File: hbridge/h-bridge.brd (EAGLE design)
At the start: 44.5 x 44.5 mm, 8 parts

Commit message: add connector parts
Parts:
- added R1, R2, R3, R4: (no value), resistor:R0603
- added U$2: JST-PH8-SMD-90, jst-ph:JST-PH-SMD-90*
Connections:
- new net N$2: R2.1, R3.1, R4.1, U$2.P$1
- net ENABLE: now also R1.2, U$2.P$8
- net GND: now also R1.1, R4.2
- net M1_DIR: now also U$2.P$6
- net M1_MOVE: now also U$2.P$7
- net M2_DIR: now also U$2.P$4
- net M2_MOVE: now also U$2.P$5
- net M3_DIR: now also U$2.P$2
- net M3_MOVE: now also U$2.P$3
- net V_RUN: now also R2.2, R3.2
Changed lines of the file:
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@@
 <element name="CHARGE" library="con-molex-micro-fit-3_0" package="43045-0206" value="" x="2.54" y="10.795" rot="R270"/>
 <element name="U$1" library="wolfbot" package="WSP1-T2-M6" value="ESWITCH-WSP1" x="2.54" y="29.21"/>
+<element name="R1" library="resistor" package="R0603" value="" x="-20.32" y="-7.62"/>
+<element name="U$2" library="jst-ph" package="JST-PH-SMD-90*" value="JST-PH8-SMD-90" x="-17.78" y="-17.78"/>
+<element name="R2" library="resistor" package="R0603" value="" x="-20.32" y="-22.86"/>
+<element name="R3" library="resistor" package="R0603" value="" x="-20.32" y="-27.94"/>
+<element name="R4" library="resistor" package="R0603" value="" x="-20.32" y="-33.02"/>
 </elements>
 <signals>
@@
 <wire x1="36.44" y1="24.765" x2="34.925" y2="26.5975" width="0.508" layer="1"/>
 <wire x1="34.925" y1="26.5975" x2="34.925" y2="40.005" width="0.508" layer="1"/>
+<contactref element="R1" pad="1"/>
+<contactref element="R4" pad="2"/>
+<wire x1="26.035" y1="30.48" x2="26.035" y2="33.02" width="0" layer="19" extent="1-1"/>
+<wire x1="21.2725" y1="8.89" x2="15.875" y2="9.525" width="0" layer="19" extent="1-1"/>
+<wire x1="23.495" y1="12.065" x2="23.495" y2="9.525" width="0" layer="19" extent="1-1"/>
+<wire x1="23.495" y1="1.905" x2="23.495" y2="4.445" width="0" layer="19" extent="1-1"/>
+<wire x1="23.495" y1="17.145" x2="23.495" y2="12.065" width="0" layer="19" extent="1-1"/>
+<wire x1="36.44" y1="16.51" x2="36.44" y2="24.765" width="0" layer="19" extent="1-1"/>
+<wire x1="-21.17" y1="-7.62" x2="8.01" y2="10.795" width="0" layer="19" extent="1-1"/>
+<wire x1="-19.47" y1="-33.02" x2="-21.17" y2="-7.62" width="0" layer="19" extent="1-1"/>
 </signal>
 <signal name="V+" class="1">
@@
 <wire x1="26.0096" y1="22.9616" x2="26.035" y2="22.86" width="0.254" layer="16"/>
 <via x="11.5062" y="32.0167" extent="1-16" drill="0.508"/>
+<contactref element="R1" pad="2"/>
+<contactref element="U$2" pad="P$8"/>
+<wire x1="-0.83" y1="-13.28" x2="13.8176" y2="20.1168" width="0" layer="19" extent="1-16"/>
+<wire x1="-19.47" y1="-7.62" x2="-0.83" y2="-13.28" width="0" layer="19" extent="1-1"/>
 </signal>
 <signal name="M1_MOVE">
@@
 <wire x1="28.067" y1="15.24" x2="26.416" y2="15.24" width="0.254" layer="16"/>
 <wire x1="18.288" y1="37.9984" x2="18.415" y2="38.1" width="0.254" layer="16"/>
+<contactref element="U$2" pad="P$7"/>
+<wire x1="-2.83" y1="-13.28" x2="6.4897" y2="18.4912" width="0" layer="19" extent="1-16"/>
 </signal>
 <signal name="M1-" class="1">
@@
 <wire x1="27.6352" y1="12.5984" x2="27.813" y2="12.7" width="0.254" layer="16"/>
 <via x="13.6144" y="17.0688" extent="1-16" drill="0.508"/>
+<contactref element="U$2" pad="P$6"/>
+<wire x1="-4.83" y1="-13.28" x2="19.1643" y2="8.128" width="0" layer="19" extent="1-16"/>
 </signal>
 <signal name="M2_DIR">
@@
 <wire x1="27.8384" y1="7.7216" x2="27.813" y2="7.62" width="0.254" layer="1"/>
 <via x="32.512" y="12.5984" extent="1-16" drill="0.508"/>
+<contactref element="U$2" pad="P$4"/>
+<wire x1="-8.83" y1="-13.28" x2="27.813" y2="7.62" width="0" layer="19" extent="1-1"/>
 </signal>
 <signal name="M2+" class="1">
@@
 <wire x1="28.067" y1="10.16" x2="28.6512" y2="10.16" width="0.254" layer="16"/>
 <wire x1="26.2128" y1="25.4" x2="26.035" y2="25.4" width="0.254" layer="16"/>
+<contactref element="U$2" pad="P$5"/>
+<wire x1="-6.83" y1="-13.28" x2="28.067" y2="10.16" width="0" layer="19" extent="1-1"/>
 </signal>
 <signal name="M3_MOVE">
@@
 <wire x1="16.0528" y1="17.0688" x2="15.875" y2="17.145" width="0.254" layer="16"/>
 <via x="21.0185" y="12.5603" extent="1-16" drill="0.508"/>
+<contactref element="U$2" pad="P$3"/>
+<wire x1="19.9771" y1="0.4572" x2="-10.83" y2="-13.28" width="0" layer="19" extent="1-1"/>
 </signal>
 <signal name="M3-" class="1">
@@
 <wire x1="27.6352" y1="2.4384" x2="25.6032" y2="0.4064" width="0.254" layer="16"/>
 <wire x1="27.6352" y1="2.4384" x2="27.813" y2="2.54" width="0.254" layer="16"/>
+<contactref element="U$2" pad="P$2"/>
+<wire x1="15.875" y1="4.445" x2="-12.83" y2="-13.28" width="0" layer="19" extent="1-1"/>
 </signal>
 <signal name="V_RUN" class="1">
@@
 <wire x1="23.368" y1="19.7104" x2="23.495" y2="19.685" width="0.508" layer="16"/>
 <via x="18.8976" y="19.9136" extent="1-16" drill="0.508"/>
+<contactref element="R2" pad="2"/>
+<contactref element="R3" pad="2"/>
+<wire x1="-19.47" y1="-22.86" x2="-19.47" y2="-27.94" width="0" layer="19" extent="1-1"/>
+<wire x1="15.875" y1="1.905" x2="-19.47" y2="-22.86" width="0" layer="19" extent="1-1"/>
 </signal>
 <signal name="V_CHARGE" class="1">
@@
 <via x="8.2296" y="32.8295" extent="1-16" drill="0.508"/>
 </signal>
+<signal name="N$2">
+<contactref element="R2" pad="1"/>
+<contactref element="R3" pad="1"/>
+<contactref element="U$2" pad="P$1"/>
+<contactref element="R4" pad="1"/>
+<wire x1="-21.17" y1="-27.94" x2="-21.17" y2="-33.02" width="0" layer="19" extent="1-1"/>
+<wire x1="-21.17" y1="-22.86" x2="-21.17" y2="-27.94" width="0" layer="19" extent="1-1"/>
+<wire x1="-14.83" y1="-13.28" x2="-21.17" y2="-22.86" width="0" layer="19" extent="1-1"/>
+</signal>
 </signals>

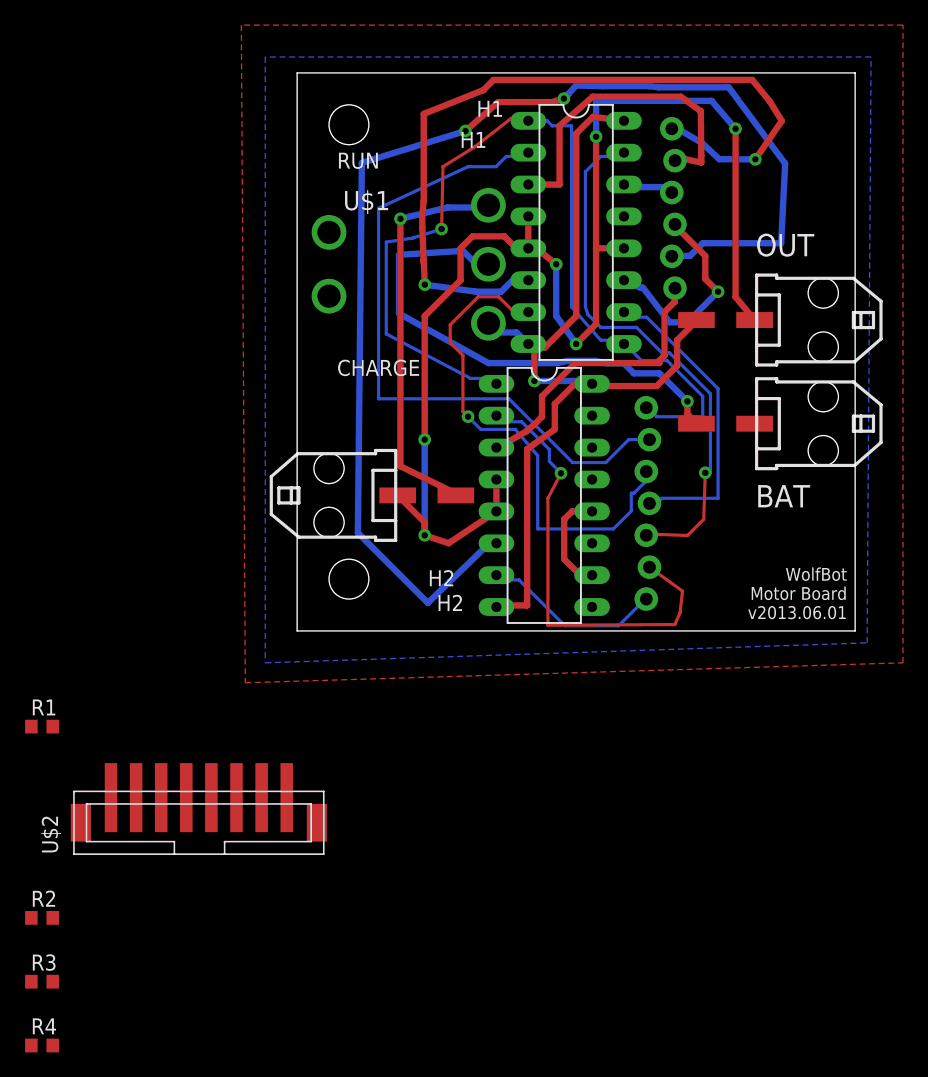
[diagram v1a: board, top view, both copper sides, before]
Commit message: tested and fixed until passed Sparkfun's DRC
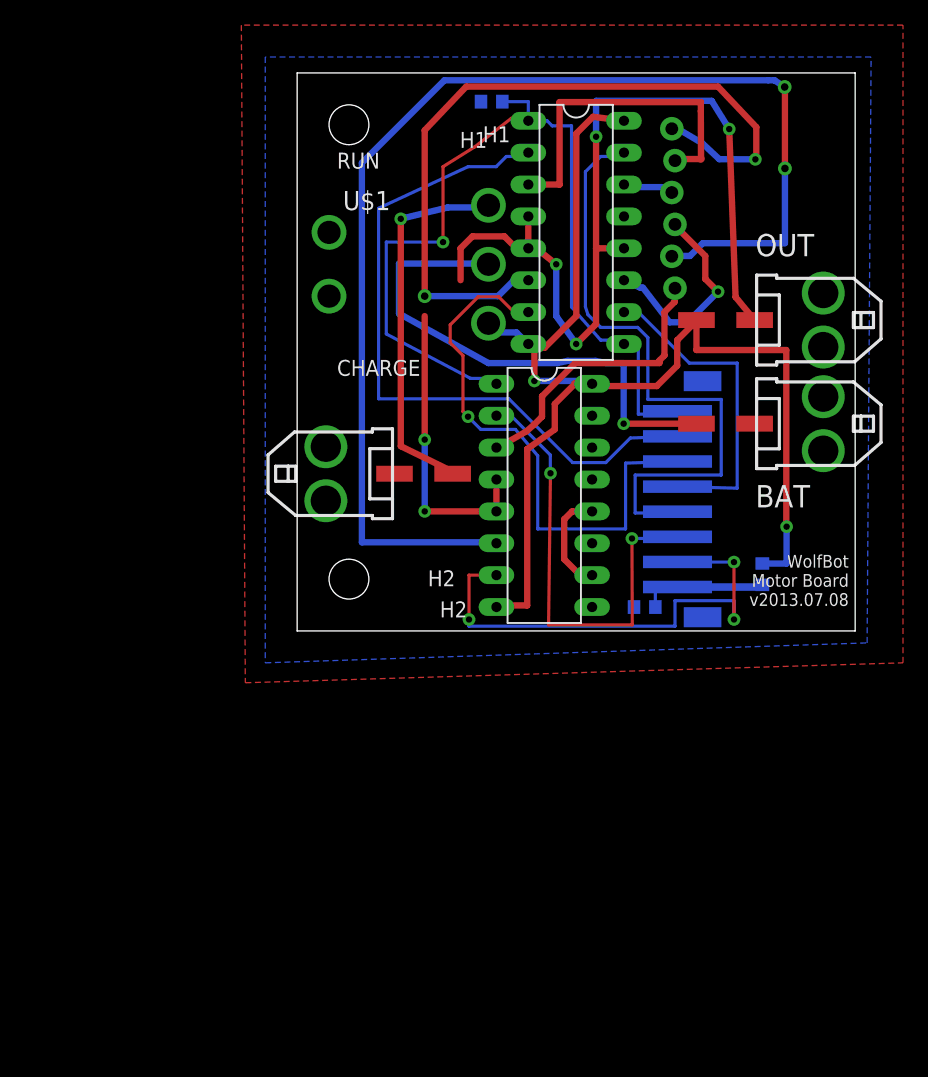
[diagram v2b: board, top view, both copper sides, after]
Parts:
- removed CONTROL: (no value), SparkFun-Connectors:1X07_LOCK
- removed R2, R3, R4: (no value), resistor:R0603
- removed U$2: JST-PH8-SMD-90, jst-ph:JST-PH-SMD-90*
- added BATT_H, BATT_L: (no value), resistor:R0603
- added U$3: JST-PH8-SMD-90, jst-ph:JST-PH-SMD-90*
- moved R1 61.3 mm to (15.5, 42.2), flipped to the bottom, turned to 180 degrees
- moved CHARGE 1.75 mm to (2.29, 12.5)
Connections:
- net ENABLE: now also U$3.P$1; no longer CONTROL.1, U$2.P$8
- net GND: now also BATT_L.2; no longer R4.2
- net M1_DIR: now also U$3.P$3; no longer CONTROL.3, U$2.P$6
- net M1_MOVE: now also U$3.P$2; no longer CONTROL.2, U$2.P$7
- net M2_DIR: now also U$3.P$5; no longer CONTROL.5, U$2.P$4
- net M2_MOVE: now also U$3.P$4; no longer CONTROL.4, U$2.P$5
- net M3_DIR: now also U$3.P$7; no longer CONTROL.7, U$2.P$2
- net M3_MOVE: now also U$3.P$6; no longer CONTROL.6, U$2.P$3
- net N$2: now also BATT_H.1, BATT_L.1, U$3.P$8; no longer R2.1, R3.1, R4.1, U$2.P$1
- net V_RUN: now also BATT_H.2; no longer R2.2, R3.2
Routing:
- net V_RUN: track 70.9 -> 99.5 mm, vias 1 -> 2
- net M3_DIR: track 14.5 -> 40.1 mm, vias 0 -> 3
- net GND: track 114.3 -> 104.2 mm
- net N$2: track 0.00 -> 10.0 mm
- net M2_DIR: track 43.1 -> 50.8 mm, vias 1 -> 0
- net M1_DIR: track 40.2 -> 44.7 mm
- net M1+: track 64.9 -> 61.4 mm
- net M1_MOVE: track 52.7 -> 55.0 mm
- net V_CHARGE: track 32.1 -> 30.5 mm
- net V+: track 39.6 -> 41.2 mm
- net M3+: track 99.1 -> 100.6 mm
- net M2_MOVE: track 24.4 -> 25.4 mm
- net M1-: track 25.9 -> 27.0 mm
- net M3_MOVE: track 36.1 -> 36.4 mm, vias 1 -> 2
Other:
- board text added: "WolfBot Motor Board v2013.07.08"
- board text removed: "WolfBot Motor Board v2013.06.01"

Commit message: mostly silkscreen fixes
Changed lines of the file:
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@@
 <layer number="50" name="dxf" color="7" fill="1" visible="no" active="no"/>
 <layer number="51" name="tDocu" color="15" fill="1" visible="yes" active="yes"/>
-<layer number="52" name="bDocu" color="14" fill="1" visible="no" active="yes"/>
+<layer number="52" name="bDocu" color="14" fill="1" visible="yes" active="yes"/>
 <layer number="53" name="tGND_GNDA" color="7" fill="9" visible="no" active="no"/>
 <layer number="54" name="bGND_GNDA" color="1" fill="9" visible="no" active="no"/>
@@
 <wire x1="17.272" y1="27.94" x2="16.002" y2="26.67" width="0.508" layer="16"/>
 <wire x1="16.002" y1="26.67" x2="10.16" y2="26.67" width="0.508" layer="16"/>
-<via x="10.16" y="26.67" extent="1-16" drill="0.6"/>
+<via x="10.16" y="26.67" extent="1-16" drill="0.508"/>
 <wire x1="10.16" y1="26.67" x2="10.16" y2="39.878" width="0.508" layer="1"/>
 <wire x1="10.16" y1="39.878" x2="13.462" y2="43.3578" width="0.508" layer="1"/>
@@
 <wire x1="38.8360875" y1="43.328971875" x2="38.8366" y2="43.2816" width="0.508" layer="1"/>
 <wire x1="38.855628125" y1="42.9514" x2="38.855628125" y2="36.84304375" width="0.508" layer="1"/>
-<via x="38.855628125" y="36.84304375" extent="1-16" drill="0.6"/>
+<via x="38.855628125" y="36.84304375" extent="1-16" drill="0.508"/>
 <wire x1="11.731371875" y1="43.862371875" x2="37.5158" y2="43.8658" width="0.508" layer="16"/>
 <wire x1="37.5158" y1="43.8658" x2="38.0238" y2="43.8658" width="0.508" layer="16"/>
 <wire x1="38.0238" y1="43.8658" x2="38.0238" y2="43.862371875" width="0.508" layer="16"/>
 <wire x1="38.0238" y1="43.862371875" x2="38.8360875" y2="43.328971875" width="0.508" layer="16"/>
-<via x="38.8360875" y="43.328971875" extent="1-16" drill="0.6"/>
+<via x="38.8360875" y="43.328971875" extent="1-16" drill="0.508"/>
 <wire x1="38.8360875" y1="43.328971875" x2="38.85854375" y2="42.995828125" width="0.508" layer="1"/>
 <wire x1="38.85854375" y1="42.995828125" x2="38.85854375" y2="43.4047" width="0.6096" layer="1"/>

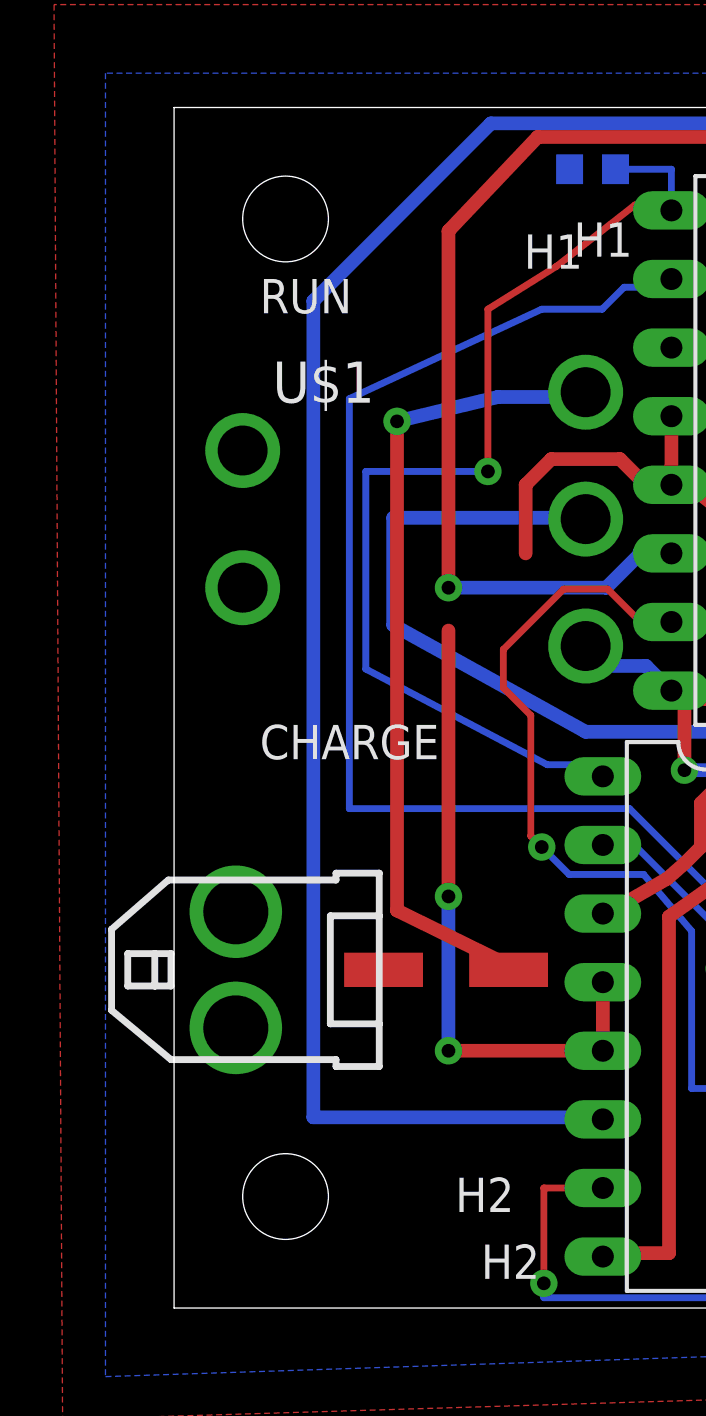
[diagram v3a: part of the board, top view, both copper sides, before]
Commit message: hole size, wire distance fixes, no soldermask changes yet
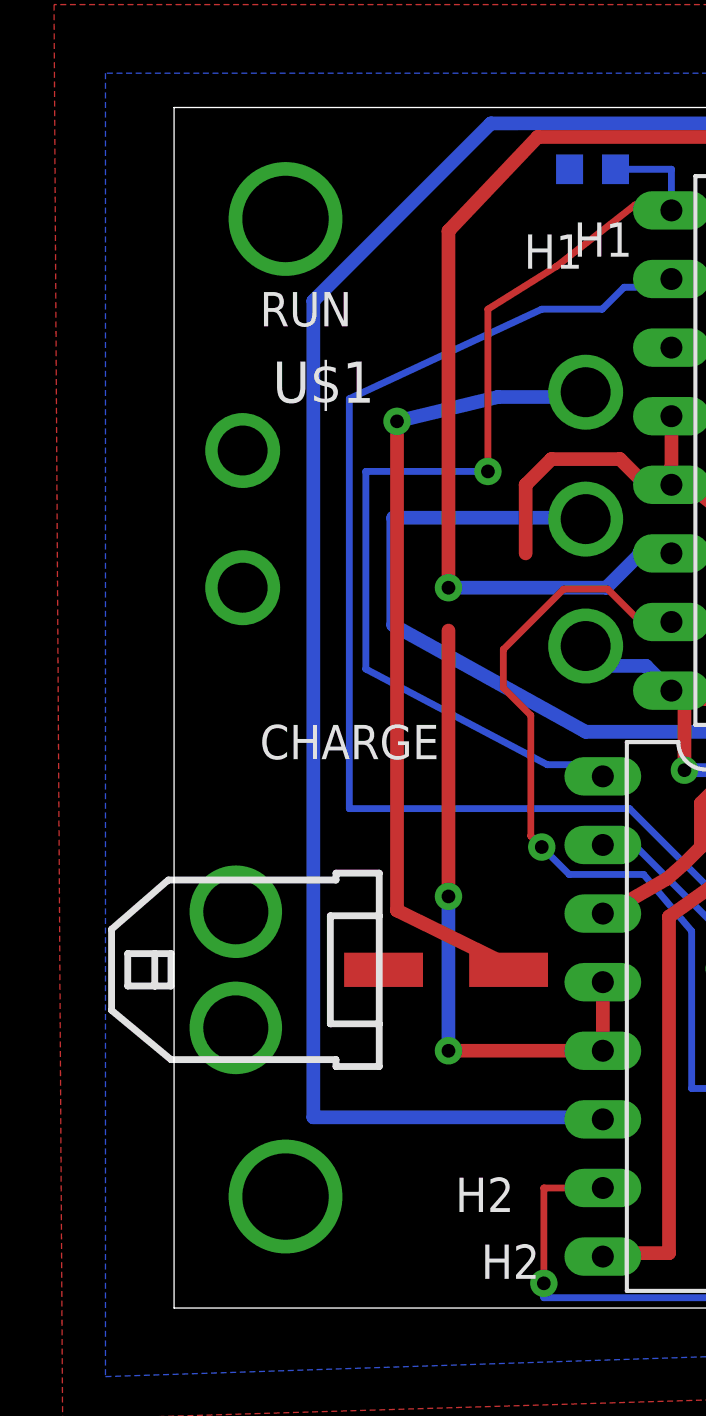
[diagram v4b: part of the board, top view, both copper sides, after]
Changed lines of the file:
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@@
 <layer number="42" name="bRestrict" color="1" fill="10" visible="no" active="yes"/>
 <layer number="43" name="vRestrict" color="2" fill="10" visible="no" active="yes"/>
-<layer number="44" name="Drills" color="7" fill="1" visible="no" active="yes"/>
-<layer number="45" name="Holes" color="7" fill="1" visible="no" active="yes"/>
+<layer number="44" name="Drills" color="7" fill="1" visible="yes" active="yes"/>
+<layer number="45" name="Holes" color="7" fill="1" visible="yes" active="yes"/>
 <layer number="46" name="Milling" color="3" fill="1" visible="no" active="yes"/>
-<layer number="47" name="Measures" color="14" fill="1" visible="yes" active="yes"/>
+<layer number="47" name="Measures" color="14" fill="1" visible="no" active="yes"/>
 <layer number="48" name="Document" color="7" fill="1" visible="yes" active="yes"/>
 <layer number="49" name="Reference" color="7" fill="1" visible="no" active="yes"/>
@@
 <layer number="122" name="_bsilk" color="7" fill="1" visible="no" active="yes"/>
 <layer number="125" name="_tNames" color="7" fill="1" visible="no" active="yes"/>
-<layer number="144" name="Drill_legend" color="7" fill="1" visible="no" active="yes"/>
+<layer number="144" name="Drill_legend" color="7" fill="1" visible="yes" active="yes"/>
 <layer number="151" name="HeatSink" color="7" fill="1" visible="no" active="yes"/>
 <layer number="199" name="Contour" color="7" fill="1" visible="no" active="yes"/>
@@
 <wire x1="44.45" y1="44.45" x2="0" y2="44.45" width="0" layer="20"/>
 <wire x1="0" y1="44.45" x2="0" y2="0" width="0" layer="20"/>
-<hole x="4.1275" y="40.3225" drill="3.175"/>
-<hole x="4.1275" y="4.1275" drill="3.175"/>
 <dimension x1="0" y1="44.45" x2="44.45" y2="44.45" x3="22.225" y3="55.7149" textsize="1.778" layer="47" unit="inch"/>
 <dimension x1="0" y1="44.45" x2="0" y2="0" x3="-20.32" y3="22.225" textsize="1.778" layer="47" unit="inch"/>
@@
 <text x="26.035" y="1.905" size="1.016" layer="22" font="vector" rot="MR0">D3</text>
 <text x="3.175" y="20.32" size="1.27" layer="21" font="vector">CHARGE</text>
-<text x="3.175" y="36.83" size="1.27" layer="21" font="vector">RUN</text>
+<text x="3.175" y="36.3474" size="1.27" layer="21" font="vector">RUN</text>
 <text x="36.5125" y="9.8425" size="1.778" layer="21" font="vector">BAT</text>
 <text x="36.5125" y="29.845" size="1.778" layer="21" font="vector">OUT</text>
@@
 <wire x1="36.8844" y1="3.497" x2="37.0586" y2="3.6712" width="0.6096" layer="16"/>
 </signal>
+<signal name="N$1">
+<via x="4.1275" y="4.1275" extent="1-16" drill="3.2"/>
+<via x="4.1275" y="40.3225" extent="1-16" drill="3.2"/>
+</signal>
 </signals>
